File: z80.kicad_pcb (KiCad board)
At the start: 2 copper layers, 118.4 x 122.9 mm, 75 parts, among them SW1 RESET, SW2 STEP, U1 Z80CPU, U2 74HC04, U3 74AC541, U4 74LS138, U5 74HC245, U6 74LS148, Y1 7.3728MHz

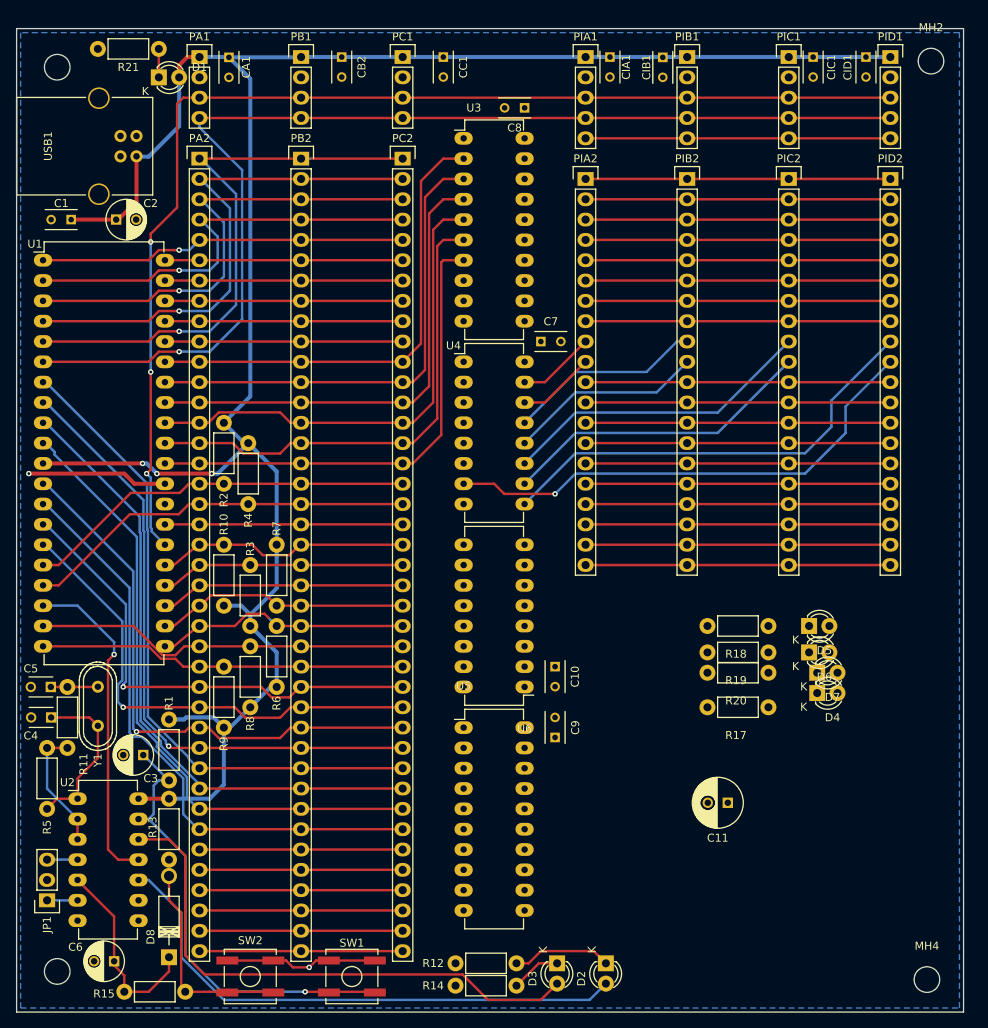
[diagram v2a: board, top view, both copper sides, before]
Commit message: Smaller, through hole, done!
Apart from maybe a few footprint issues and a bit of trace fiddling this
should be pretty close. Be interesting how much this will cost now. :)
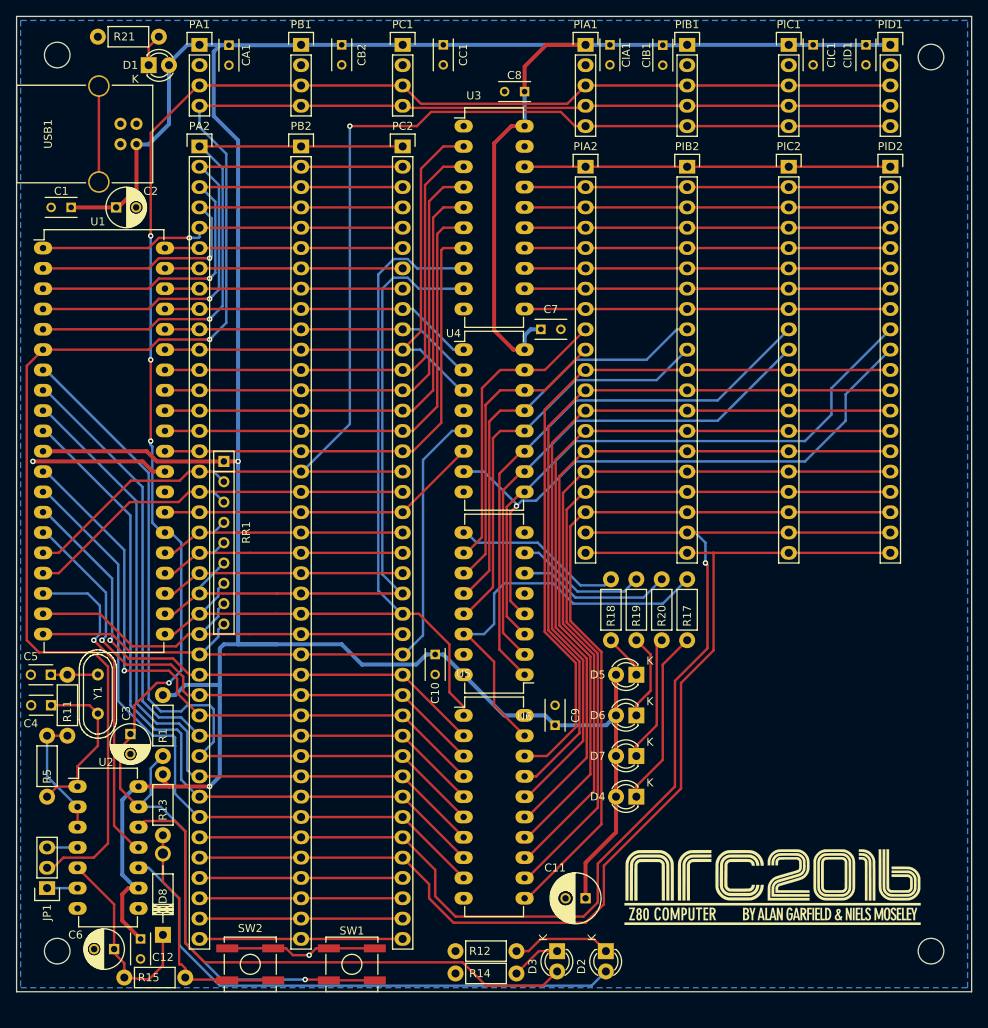
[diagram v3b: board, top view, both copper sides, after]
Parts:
- removed R10, R2, R3, R4, R6, R7, R8, R9: 10K, Resistors_ThroughHole:Resistor_Horizontal_RM7mm
- added C12: 100nF, Capacitors_ThroughHole:C_Rect_L4_W2.5_P2.5, F.Cu at (56.1, 145.8)
- added G***: LOGO, ncr2016_logo:nrc2016_logo_1600, F.Cu at (135.1, 139.4)
- added RR1: RR8, Resistors_ThroughHole:Resistor_Array_SIP8, F.Cu at (66.5, 96.3)
- moved D4 26.1 mm to (118.1, 128.0), turned to 180 degrees
- moved D7 24.9 mm to (118.1, 122.9), turned to 180 degrees
- moved D6 23.0 mm to (118.1, 117.9), turned to 180 degrees
- moved D5 22.4 mm to (118.1, 112.8), turned to 180 degrees
- moved C11 21.4 mm to (111.8, 140.7)
- moved R18 19.8 mm to (114.9, 108.5), turned to 90 degrees
- moved R19 16.6 mm to (118.1, 108.5), turned to 90 degrees
- moved C10 15.1 mm to (93.0, 110.2)
- moved R20 13.9 mm to (121.3, 108.5), turned to 90 degrees
- moved R17 13.2 mm to (124.5, 108.5), turned to 90 degrees
- moved MH4 3.59 mm to (154.9, 147.3)
- moved R13 3.14 mm to (58.9, 125.2)
- moved R1 3.14 mm to (58.9, 115.3)
- moved C3 3.08 mm to (54.9, 120.2), turned to 270 degrees
- moved D8 2.90 mm to (58.9, 145.3)
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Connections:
- U2 pad 9: (no net) -> VCC
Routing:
- net VCC: track 272.0 -> 423.0 mm, vias 3 -> 2
- net /S1: track 63.5 -> 148.2 mm, vias 0 -> 1
- net /S2: track 63.5 -> 143.6 mm
- net /~INT: track 88.1 -> 167.7 mm, vias 0 -> 1
- net /~CLK: track 140.8 -> 219.1 mm
- net /~RD: track 32.8 -> 109.5 mm
- net /IO/D0-B: track 38.1 -> 94.5 mm
- net /IO/D1-B: track 38.1 -> 93.7 mm
- net /IO/D6-B: track 38.1 -> 93.0 mm
- net /IO/D7-B: track 38.1 -> 93.0 mm
- net /IO/D3-B: track 38.1 -> 93.0 mm
- net /IO/D2-B: track 38.1 -> 93.0 mm
- net /IO/D4-B: track 38.1 -> 93.0 mm
- net /IO/D5-B: track 38.1 -> 93.0 mm
- net /~WR: track 31.9 -> 86.4 mm
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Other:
- board size 118.4 x 122.9 mm -> 119.4 x 121.9 mm

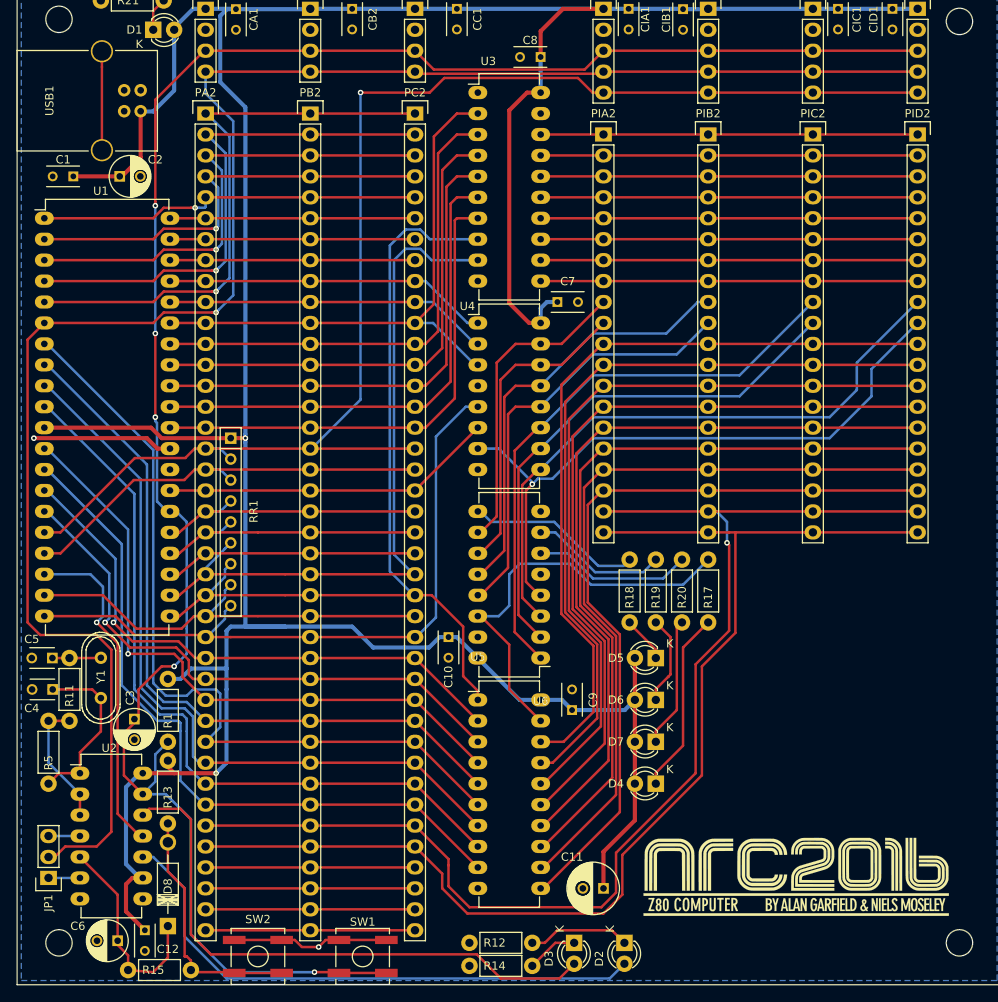
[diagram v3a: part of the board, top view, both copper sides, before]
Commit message: Change to 7 mils clearance to make cheaper
7 mils seems to be the minimum clearance for the cheap board houses. So
reworked the board to match.
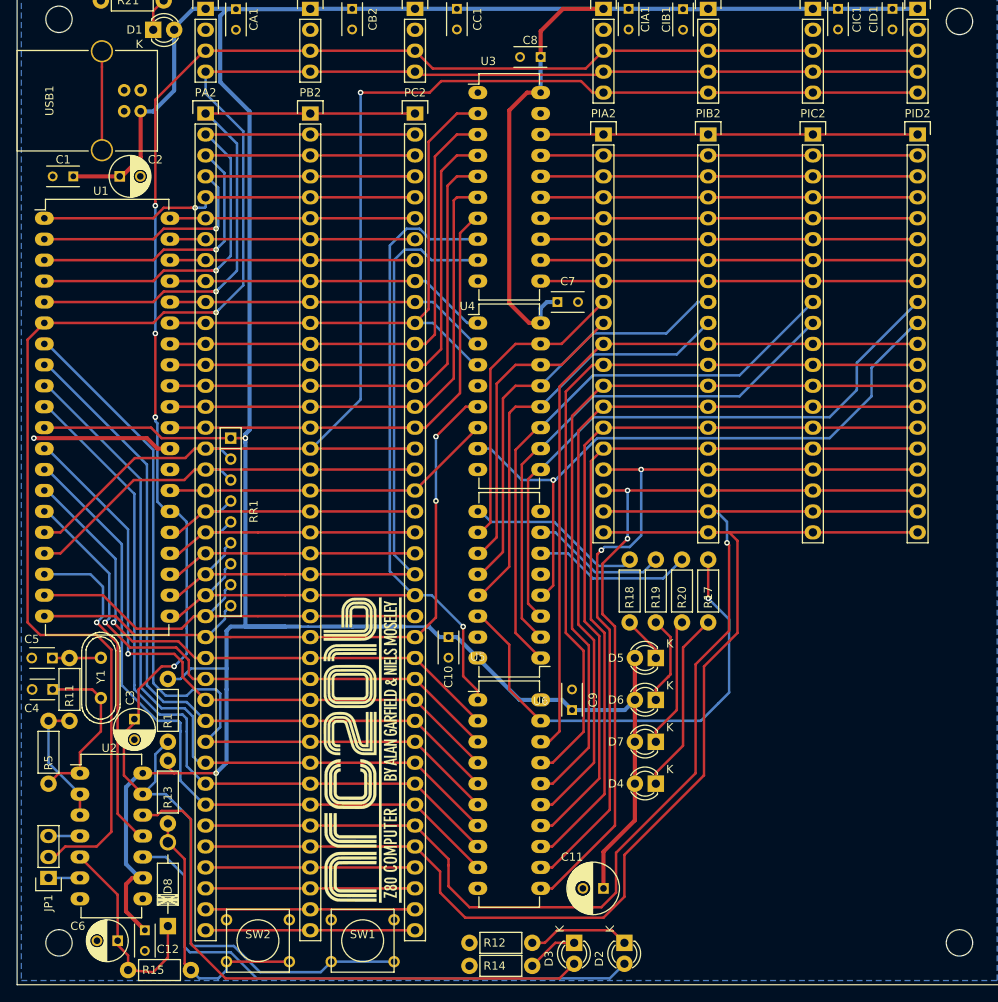
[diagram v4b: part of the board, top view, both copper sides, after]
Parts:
- SW1, SW2: footprint Buttons_Switches_SMD:SW_SPST_B3SL-1002P -> Buttons_Switches_ThroughHole:SW_PUSH_SMALL
- moved G*** 54.7 mm to (82.7, 124.0), turned to 90 degrees
- moved SW1 1.91 mm to (82.5, 147.1)
- moved SW2 1.91 mm to (69.8, 147.1)
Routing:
- net GND: track 36.3 -> 17.1 mm, vias 2 -> 1
- net /IO/~BUS_EN: track 51.2 -> 57.5 mm, vias 0 -> 1
- net /IO/D0-B: track 94.5 -> 90.2 mm
- net /IO/D6-B: track 93.0 -> 95.8 mm, vias 0 -> 2
- net Net-(D8-Pad2): track 30.2 -> 32.7 mm
- net /~RESET: track 242.7 -> 244.7 mm, vias 5 -> 4
- net /S2: track 143.6 -> 145.3 mm
- net Net-(D2-Pad2): track 68.7 -> 70.3 mm
- net /A0: track 60.5 -> 59.2 mm
- net /~CLK: track 219.1 -> 220.2 mm
- net /IO/D5-B: track 93.0 -> 92.2 mm
- net /IO/D4-B: track 93.0 -> 92.2 mm
- net /A15: track 70.3 -> 71.1 mm
- net /IO/D3-B: track 93.0 -> 92.4 mm
- net VCC: track 423.0 -> 422.4 mm
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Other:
- net class Default: clearance 0.1524 -> 0.1778
- net class power: clearance 0.1524 -> 0.1778
- rule trace_clearance: 0.1524 -> 0.1778
- rule trace_min: 0.1524 -> 0.1778

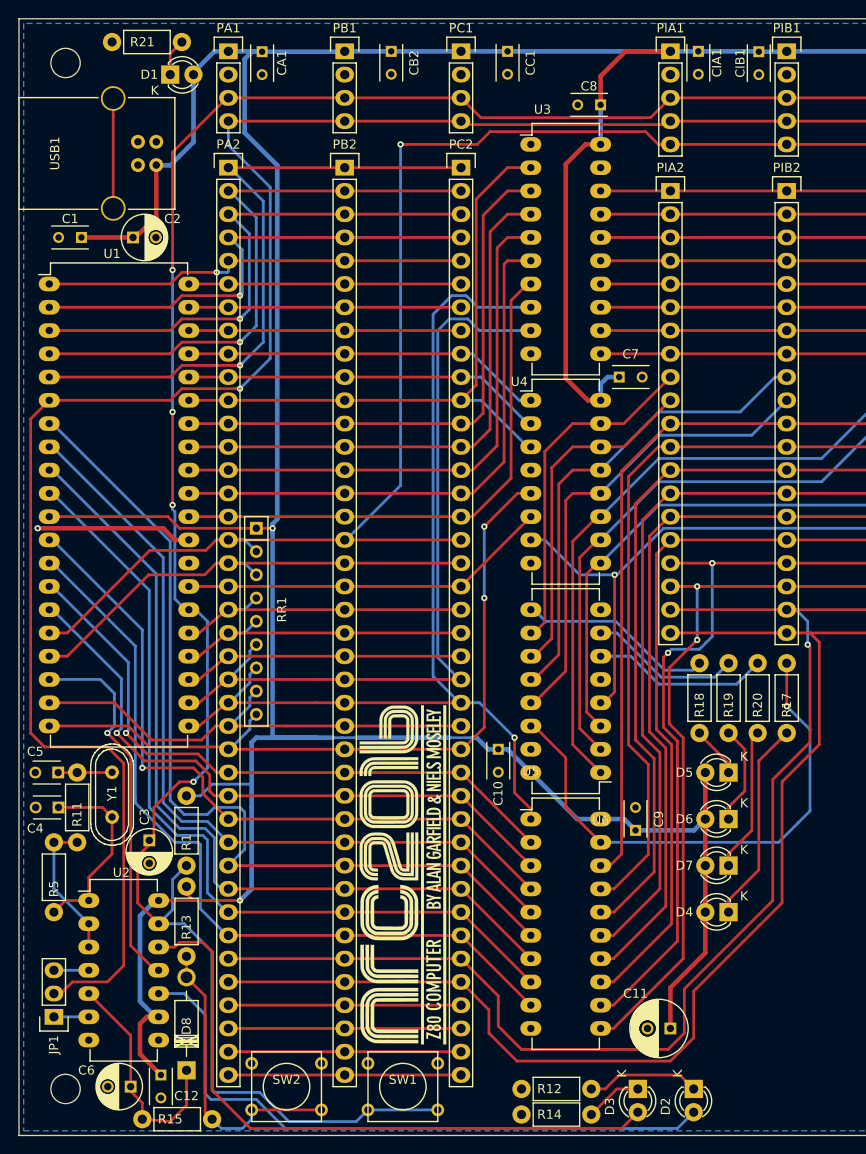
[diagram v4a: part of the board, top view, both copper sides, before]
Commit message: Few more trace tweaks, gave xtal more space.
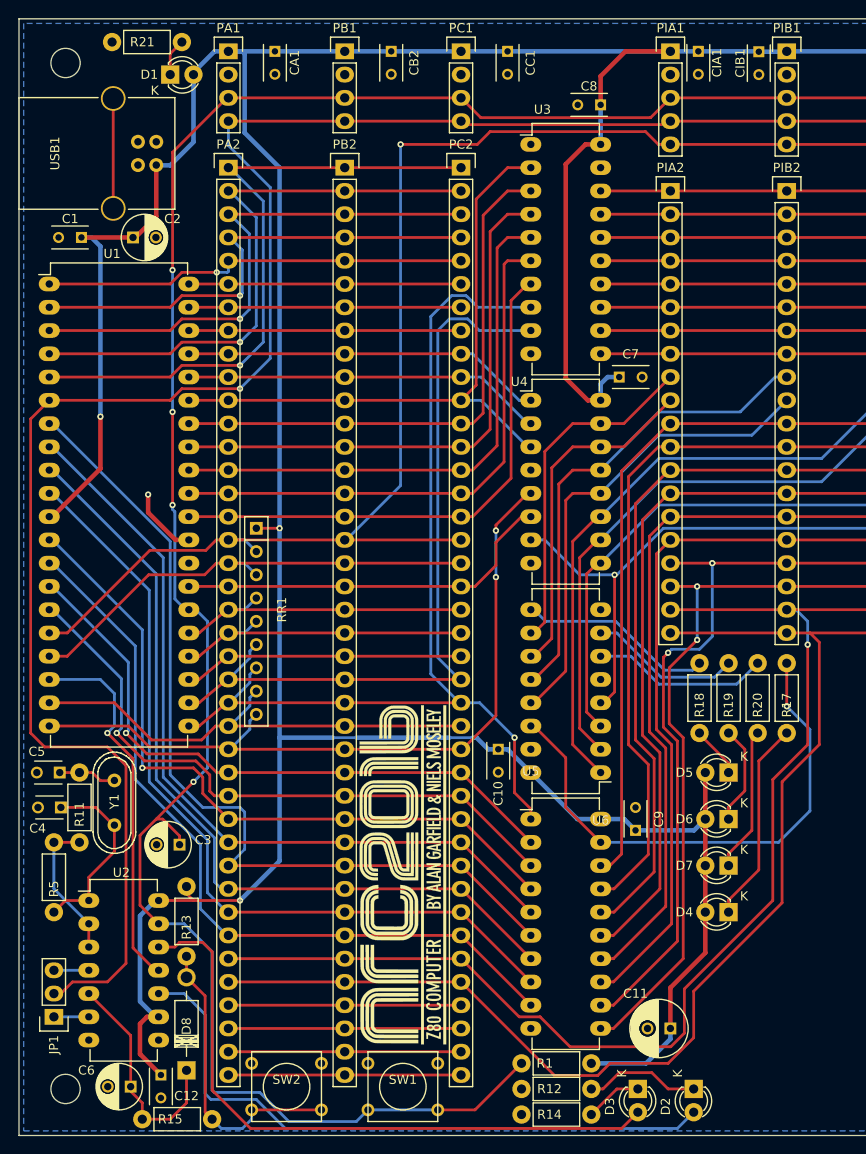
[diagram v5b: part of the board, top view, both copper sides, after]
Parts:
- moved R1 53.0 mm to (103.1, 144.5), turned to 180 degrees
- moved C3 3.34 mm to (58.2, 120.7), turned to 180 degrees
- moved CA1 1.40 mm to (68.6, 34.0)
- moved Y1 0.92 mm to (51.1, 116.1)
- moved C4 0.25 mm to (45.2, 116.6)
- moved R11 0.25 mm to (47.2, 120.4)
- moved C5 0.17 mm to (45.1, 112.8)
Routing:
- net GND: track 17.1 -> 7.76 mm
- net VCC: track 422.4 -> 431.6 mm, vias 2 -> 3
- net /~RESET: track 244.7 -> 251.4 mm
- net /S1: track 148.2 -> 145.8 mm
- net /D4: track 98.9 -> 96.6 mm
- net /D6: track 91.9 -> 90.3 mm
- net /D5: track 92.3 -> 90.6 mm
- net /D3: track 89.3 -> 87.7 mm
- net /~M1: track 40.6 -> 42.1 mm
- net /D7: track 86.7 -> 85.2 mm
- net Net-(C4-Pad1): track 21.3 -> 20.6 mm
- net /~IORQ: track 83.2 -> 82.6 mm

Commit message: ugh another tweak. OCD will kill me.
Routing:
- net /IO/D1-B: track 93.1 -> 92.4 mm
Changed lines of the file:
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@@
     (thickness 1.6002)
     (drawings 6)
-    (tracks 861)
+    (tracks 860)
     (zones 0)
     (modules 70)
@@
   (segment (start 59.182 64.516) (end 63.5 64.516) (width 0.3048) (layer Top) (net 22) (status 30))
   (segment (start 76.2 64.516) (end 88.9 64.516) (width 0.3048) (layer Top) (net 22) (status 30))
-  (segment (start 88.9 67.056) (end 90.17 67.056) (width 0.3048) (layer Bottom) (net 23) (status 10))
-  (segment (start 90.17 67.056) (end 95.25 72.136) (width 0.3048) (layer Bottom) (net 23))
-  (segment (start 95.25 72.136) (end 96.52 72.136) (width 0.3048) (layer Bottom) (net 23) (status 20))
+  (segment (start 88.9 67.056) (end 91.059 67.056) (width 0.3048) (layer Bottom) (net 23))
+  (segment (start 91.059 67.056) (end 96.139 72.136) (width 0.3048) (layer Bottom) (net 23))
+  (segment (start 96.139 72.136) (end 96.52 72.136) (width 0.3048) (layer Bottom) (net 23))
   (segment (start 76.2 67.056) (end 88.9 67.056) (width 0.3048) (layer Top) (net 23) (status 30))
   (segment (start 63.5 67.056) (end 76.2 67.056) (width 0.3048) (layer Top) (net 23) (status 30))
@@
   (segment (start 124.46 74.676) (end 137.16 74.676) (width 0.3048) (layer Top) (net 67) (status 30))
   (segment (start 111.76 74.676) (end 124.46 74.676) (width 0.3048) (layer Top) (net 67) (status 30))
-  (segment (start 111.76 77.216) (end 110.4392 77.216) (width 0.3048) (layer Top) (net 68) (status 10))
-  (segment (start 110.4392 77.216) (end 107.188 80.4672) (width 0.3048) (layer Top) (net 68))
-  (segment (start 107.188 80.4672) (end 107.188 109.728) (width 0.3048) (layer Top) (net 68))
+  (segment (start 111.76 77.216) (end 111.633 77.216) (width 0.3048) (layer Top) (net 68))
   (segment (start 107.188 109.728) (end 109.347 111.887) (width 0.3048) (layer Top) (net 68))
+  (segment (start 111.633 77.216) (end 107.188 81.661) (width 0.3048) (layer Top) (net 68))
+  (segment (start 105.5948 125.476) (end 104.14 125.476) (width 0.3048) (layer Top) (net 68))
+  (segment (start 107.188 81.661) (end 107.188 109.728) (width 0.3048) (layer Top) (net 68))
   (segment (start 109.347 111.887) (end 109.347 121.7238) (width 0.3048) (layer Top) (net 68))
-  (segment (start 105.5948 125.476) (end 104.14 125.476) (width 0.3048) (layer Top) (net 68) (status 20))
   (segment (start 109.347 121.7238) (end 105.5948 125.476) (width 0.3048) (layer Top) (net 68))
   (segment (start 111.76 77.216) (end 111.6076 77.216) (width 0.3048) (layer Top) (net 68) (status 30))
@@
   (segment (start 124.46 82.296) (end 137.16 82.296) (width 0.3048) (layer Top) (net 70) (status 30))
   (segment (start 111.76 82.296) (end 124.46 82.296) (width 0.3048) (layer Top) (net 70) (status 30))
-  (segment (start 104.14 133.096) (end 105.537 133.096) (width 0.3048) (layer Top) (net 71) (status 10))
+  (segment (start 109.474 108.331) (end 109.474 86.9696) (width 0.3048) (layer Top) (net 71))
   (segment (start 105.537 133.096) (end 111.252 127.381) (width 0.3048) (layer Top) (net 71))
-  (segment (start 111.252 127.381) (end 111.252 110.109) (width 0.3048) (layer Top) (net 71))
+  (segment (start 111.6076 84.836) (end 111.76 84.836) (width 0.3048) (layer Top) (net 71) (status 30))
   (segment (start 111.252 110.109) (end 109.474 108.331) (width 0.3048) (layer Top) (net 71))
-  (segment (start 109.474 108.331) (end 109.474 86.9696) (width 0.3048) (layer Top) (net 71))
+  (segment (start 111.252 127.381) (end 111.252 110.109) (width 0.3048) (layer Top) (net 71))
   (segment (start 109.474 86.9696) (end 111.6076 84.836) (width 0.3048) (layer Top) (net 71) (status 20))
-  (segment (start 111.6076 84.836) (end 111.76 84.836) (width 0.3048) (layer Top) (net 71) (status 30))
+  (segment (start 104.14 133.096) (end 105.537 133.096) (width 0.3048) (layer Top) (net 71) (status 10))
   (segment (start 104.14 133.096) (end 104.49 133.096) (width 0.3048) (layer Top) (net 71) (status 30))
   (segment (start 137.16 84.836) (end 149.86 84.836) (width 0.3048) (layer Top) (net 71) (status 30))
@@
   (segment (start 110.236 88.9) (end 111.76 87.376) (width 0.3048) (layer Top) (net 72) (status 20))
   (segment (start 104.49 135.636) (end 104.14 135.636) (width 0.3048) (layer Top) (net 72) (status 30))
-  (segment (start 111.76 87.376) (end 111.6076 87.376) (width 0.3048) (layer Top) (net 72) (status 30))
   (segment (start 137.16 87.376) (end 149.86 87.376) (width 0.3048) (layer Top) (net 72) (status 30))
   (segment (start 124.46 87.376) (end 137.16 87.376) (width 0.3048) (layer Top) (net 72) (status 30))
